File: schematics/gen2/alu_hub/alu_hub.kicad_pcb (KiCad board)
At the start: 2 copper layers, 100 x 91.1 mm, 23 parts, among them U1 74LS574, U10 74LS02, U2 74LS245, U3 74LS02, U4 74LS181, U5 74LS181, U6 74LS574, U7 74LS245, U8 74LS245, U9 74LS02

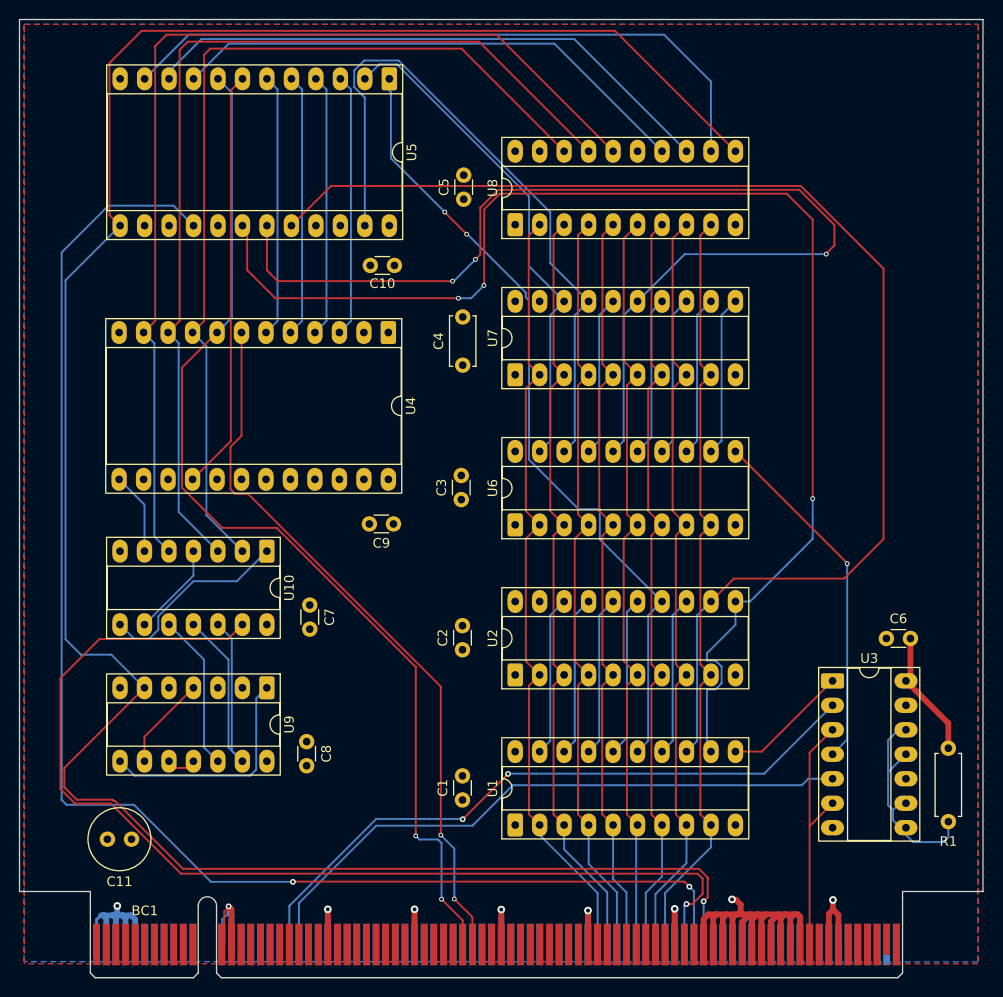
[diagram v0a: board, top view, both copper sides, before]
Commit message: inprgress(alu); 9 traces left
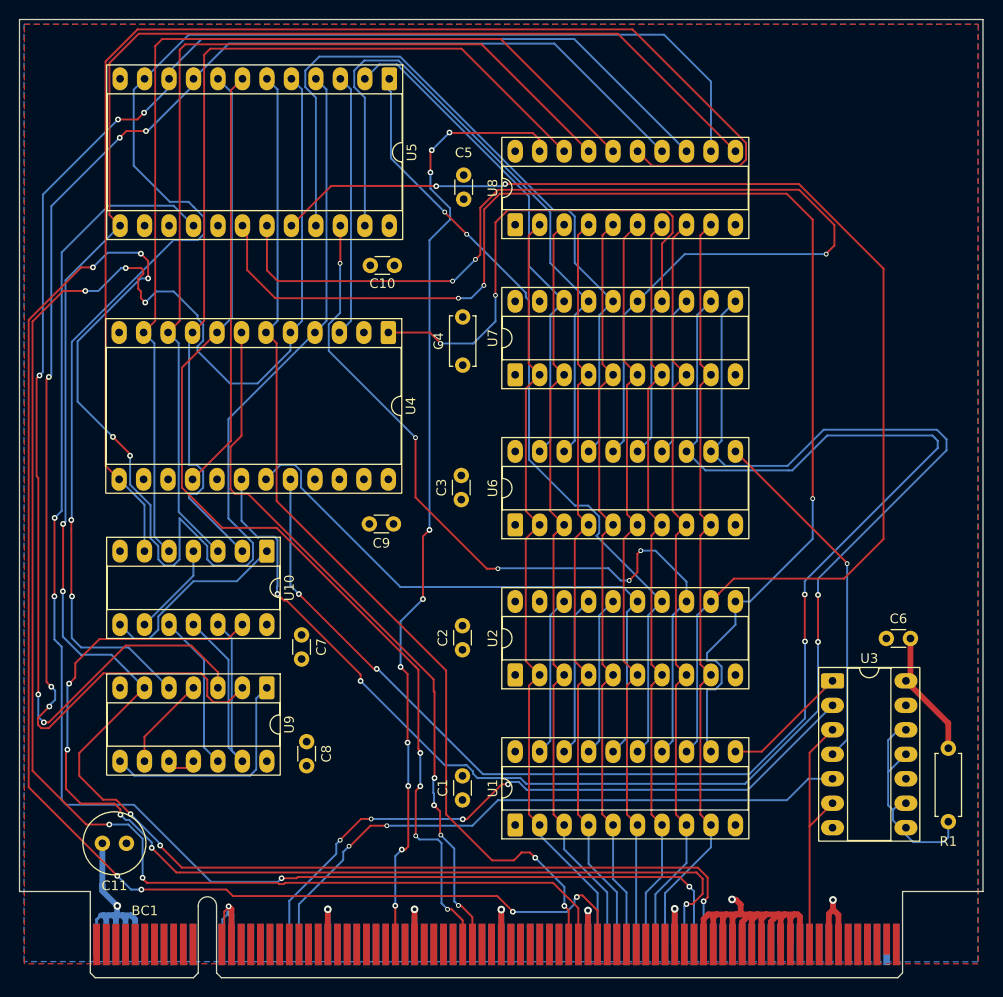
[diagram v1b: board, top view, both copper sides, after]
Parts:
- moved C7 3.22 mm to (129.3, 108.4)
- moved C11 0.68 mm to (111.1, 130.0)
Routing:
- net Net-(BC1-ALUS2): track 27.3 -> 245.0 mm, vias 0 -> 9
- net Net-(BC1-ALUS1): track 27.3 -> 186.0 mm, vias 0 -> 5
- net /LOW7: track 16.6 -> 159.9 mm, vias 0 -> 4
- net /LOW6: track 16.6 -> 154.7 mm, vias 0 -> 4
- net Net-(U4-F3): track 8.54 -> 139.1 mm
- net Net-(U5-F0): track 54.8 -> 157.2 mm, vias 0 -> 5
- net Net-(BC1-~{RALU}): track 0.00 -> 100.1 mm, vias 0 -> 10
- net Net-(U5-F1): track 60.7 -> 158.8 mm, vias 0 -> 5
- net Net-(U5-F2): track 69.9 -> 152.1 mm, vias 0 -> 2
- net Net-(BC1-ALUS0): track 27.3 -> 107.3 mm, vias 0 -> 2
- net /HIGH5: track 16.6 -> 86.6 mm, vias 0 -> 5
- net /LOW2: track 16.6 -> 79.1 mm
- net /LOW4: track 16.6 -> 68.0 mm, vias 0 -> 2
- net /HIGH3: track 16.6 -> 62.7 mm
- net VCC: track 33.0 -> 40.5 mm
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
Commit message: alu hub done
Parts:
- C1, C10, C2, C3, C6, C7, C8, C9: footprint Capacitor_THT:C_Disc_D3.0mm_W1.6mm_P2.50mm -> Capacitor_THT:C_Disc_D5.0mm_W2.5mm_P5.00mm
- C5: footprint Capacitor_THT:C_Disc_D3.0mm_W1.6mm_P2.50mm -> Capacitor_THT:C_Disc_D5.0mm_W2.5mm_P2.50mm
- moved C1 62.1 mm to (146.3, 63.4)
- moved C5 54.5 mm to (146.9, 117.6), turned to -90 degrees
- moved C4 30.7 mm to (146.0, 111.1)
- moved C2 29.3 mm to (146.7, 80.6)
- moved C9 17.5 mm to (125.5, 110.6)
- moved C7 13.5 mm to (134.9, 96.1), turned to 0 degrees
- moved C8 10.6 mm to (121.1, 125.5), turned to 0 degrees
- moved C3 9.20 mm to (145.6, 85.1), turned to 0 degrees
- moved C6 5.71 mm to (192.4, 103.6), turned to -90 degrees
- moved C10 0.85 mm to (135.6, 69.7)
- moved C11 0.14 mm to (111.1, 130.1)
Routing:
- net Net-(BC1-~{RARGL}): track 0.00 -> 183.5 mm, vias 0 -> 7
- net Net-(BC1-ALUS3): track 27.3 -> 193.2 mm, vias 0 -> 10
- net /LOW5: track 16.6 -> 90.7 mm, vias 0 -> 5
- net /HIGH0: track 16.6 -> 87.5 mm, vias 0 -> 3
- net Net-(BC1-~{RARGH}): track 0.00 -> 65.3 mm, vias 0 -> 9
- net /HIGH1: track 16.6 -> 72.9 mm, vias 0 -> 4
- net /HIGH2: track 16.6 -> 70.1 mm, vias 0 -> 4
- net VCC: track 40.5 -> 87.0 mm
- net /LOW7: track 159.9 -> 172.5 mm, vias 4 -> 8
- net /LOW6: track 154.7 -> 166.3 mm, vias 4 -> 8
- net /HIGH5: track 86.6 -> 84.0 mm
- net /HIGH3: track 62.7 -> 64.0 mm, vias 0 -> 4
- net /HIGH4: track 83.7 -> 84.0 mm, vias 2 -> 4
- net /HIGH7: track 138.0 -> 138.3 mm, vias 3 -> 5
- net /LOW3: track 113.9 -> 114.0 mm, vias 3 -> 5
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
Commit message: alu review
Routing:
- net Net-(R1-Pad2): track 24.0 -> 16.4 mm
- net Net-(BC1-~{CLK}): track 26.6 -> 25.0 mm
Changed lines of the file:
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@@
 	)
 	(segment
-		(start 182 128.22)
-		(end 184.38 125.84)
-		(width 0.2)
+		(start 186.5 123.72)
+		(end 186.5 120.34)
+		(width 0.4)
 		(layer "F.Cu")
 		(net 40)
 	)
 	(segment
-		(start 182 120.6)
-		(end 184.38 118.22)
-		(width 0.2)
+		(start 184.38 125.84)
+		(end 186.5 123.72)
+		(width 0.4)
 		(layer "F.Cu")
 		(net 40)
@@
 		(start 182 140.5)
 		(end 182 128.22)
-		(width 0.2)
+		(width 0.4)
 		(layer "F.Cu")
 		(net 40)
@@
 	(segment
 		(start 182 128.22)
-		(end 182 120.6)
-		(width 0.2)
+		(end 184.38 125.84)
+		(width 0.4)
+		(layer "F.Cu")
+		(net 40)
+	)
+	(segment
+		(start 186.5 120.34)
+		(end 184.38 118.22)
+		(width 0.4)
 		(layer "F.Cu")
 		(net 40)
@@
 	)
 	(segment
-		(start 169.3 136.925)
-		(end 169.475 136.75)
-		(width 0.2)
-		(layer "F.Cu")
-		(net 88)
-	)
-	(segment
 		(start 169.325 136.95)
 		(end 169.3 136.925)
@@
 	)
 	(segment
-		(start 191.23 118.22)
-		(end 192 118.22)
+		(start 192 118.22)
+		(end 192 120.76)
 		(width 0.2)
 		(layer "B.Cu")
@@
 	)
 	(segment
-		(start 190.15 126.05)
+		(start 190.15 123.99)
 		(end 190.15 122.61)
 		(width 0.2)
@@
 	)
 	(segment
-		(start 192.75 129.875)
-		(end 192 129.125)
-		(width 0.2)
-		(layer "B.Cu")
-		(net 104)
-	)
-	(segment
-		(start 190.15 122.61)
-		(end 190.15 119.3)
-		(width 0.2)
-		(layer "B.Cu")
-		(net 104)
-	)
-	(segment
-		(start 195.9 129.875)
-		(end 192.75 129.875)
-		(width 0.2)
-		(layer "B.Cu")
-		(net 104)
-	)
-	(segment
-		(start 196.4 129.375)
-		(end 195.9 129.875)
-		(width 0.2)
-		(layer "B.Cu")
-		(net 104)
-	)
-	(segment
-		(start 192 129.125)
-		(end 192 128.38)
-		(width 0.2)
-		(layer "B.Cu")
-		(net 104)
-	)
-	(segment
-		(start 191.43 128.38)
-		(end 190.65 127.6)
-		(width 0.2)
-		(layer "B.Cu")
-		(net 104)
-	)
-	(segment
-		(start 190.65 126.55)
-		(end 190.15 126.05)
-		(width 0.2)
-		(layer "B.Cu")
-		(net 104)
-	)
-	(segment
-		(start 190.65 126.55)
-		(end 191.36 125.84)
-		(width 0.2)
-		(layer "B.Cu")
-		(net 104)
-	)
-	(segment
-		(start 191.36 125.84)
-		(end 192 125.84)
-		(width 0.2)
-		(layer "B.Cu")
-		(net 104)
-	)
-	(segment
-		(start 196.4 127.75)
-		(end 196.4 129.375)
+		(start 195.77 128.38)
+		(end 196.4 127.75)
 		(width 0.2)
 		(layer "B.Cu")
@@
 	(segment
 		(start 192 128.38)
-		(end 191.43 128.38)
+		(end 195.77 128.38)
 		(width 0.2)
 		(layer "B.Cu")
@@
 	)
 	(segment
-		(start 190.15 119.3)
-		(end 191.23 118.22)
+		(start 190.15 122.61)
+		(end 192 120.76)
 		(width 0.2)
 		(layer "B.Cu")
@@
 	)
 	(segment
-		(start 190.15 122.61)
-		(end 192 120.76)
+		(start 192 125.84)
+		(end 190.15 123.99)
 		(width 0.2)
 		(layer "B.Cu")
@@
 	)
 	(segment
-		(start 190.65 127.6)
-		(end 190.65 126.55)
+		(start 192 125.84)
+		(end 192 128.38)
 		(width 0.2)
 		(layer "B.Cu")

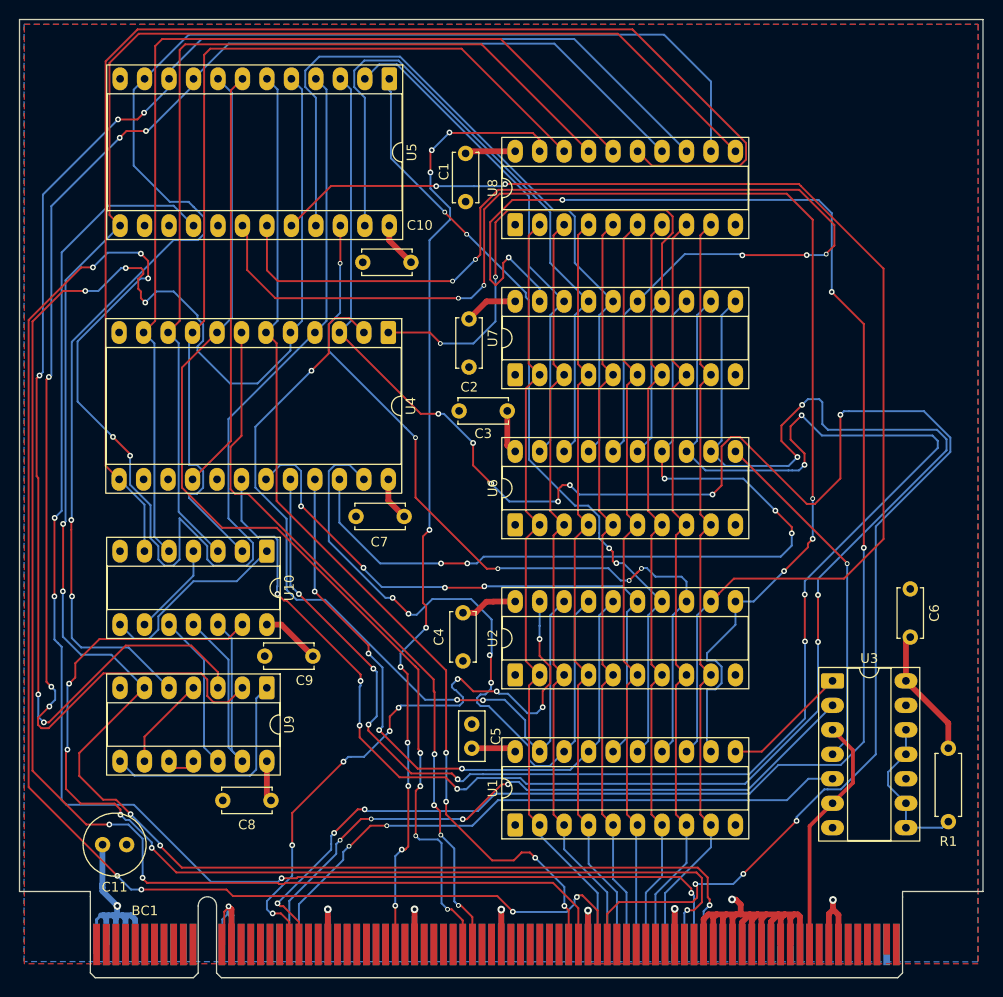
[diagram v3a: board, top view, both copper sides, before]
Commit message: chore(alu hub): changed logo and text
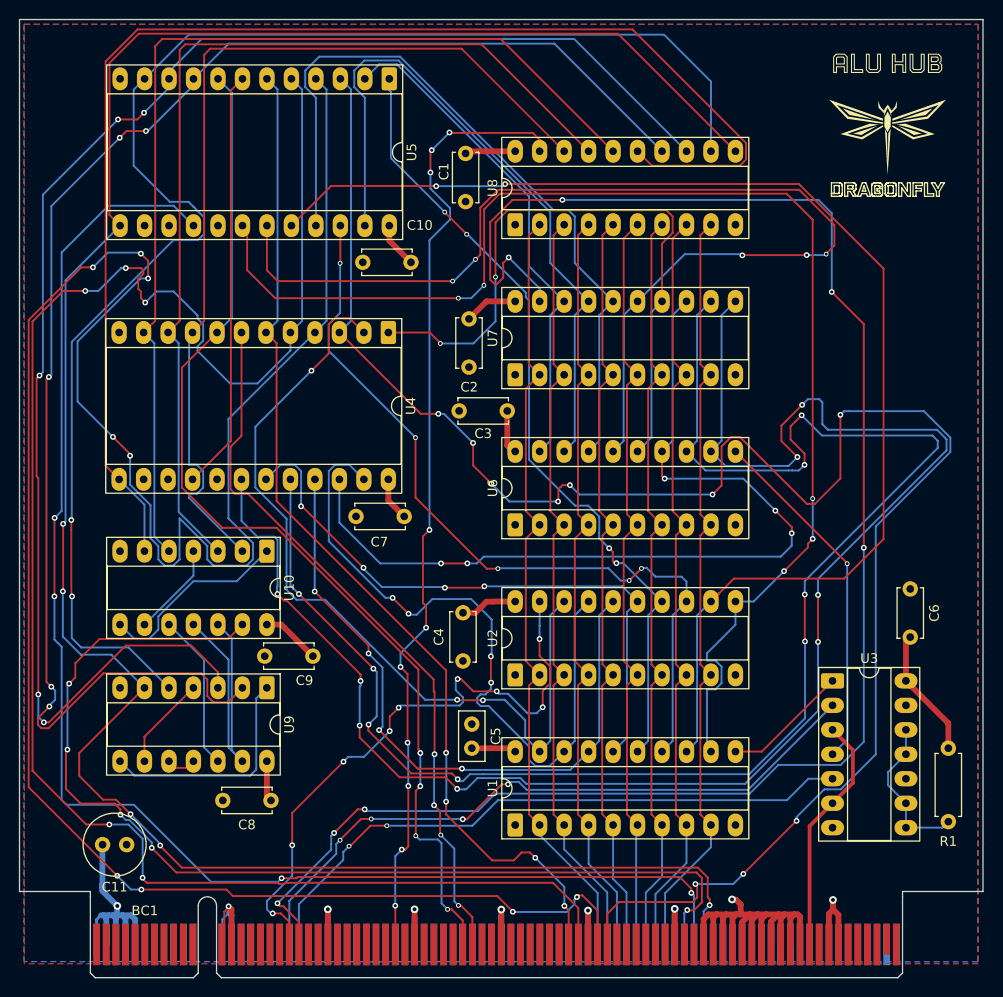
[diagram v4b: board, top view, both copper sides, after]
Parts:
- added kibuzzard-6911C7CA: G***, kibuzzard-6911C7CA, F.Cu at (190.1, 49.0)

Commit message: chore(kicad-pcb): added apps ucu logo
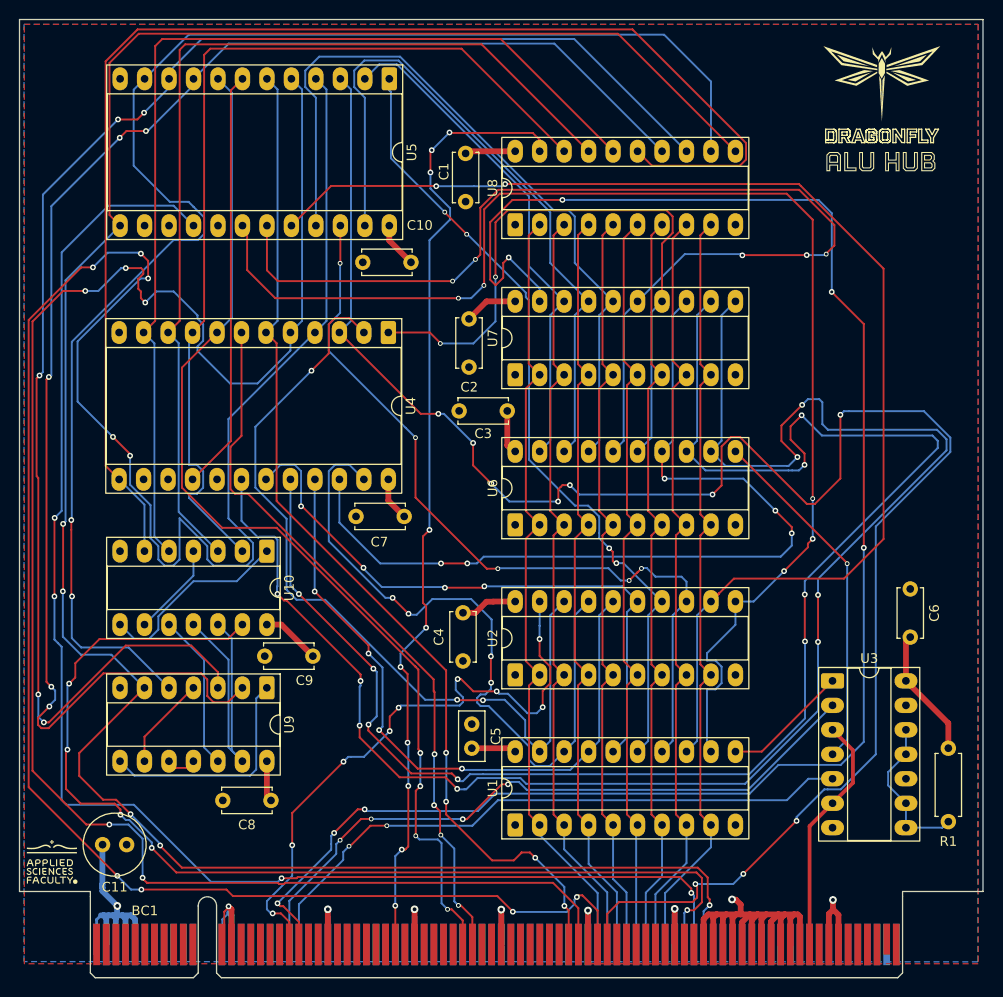
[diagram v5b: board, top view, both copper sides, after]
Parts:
- moved kibuzzard-6911C7CA 10.2 mm to (189.4, 59.2)
